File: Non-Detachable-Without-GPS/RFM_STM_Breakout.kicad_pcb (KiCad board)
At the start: 2 copper layers, 58 x 48.3 mm, 29 parts, among them J1 USB_B_Micro, J2 Conn_01x02_Male, J3 Conn_01x16_Male, J4 Conn_01x12_Male, J5 Conn_01x15_Male, J6 Conn_Coaxial, SW1 SW_Push, U1 RFM95W-868S2, U2 XC6206P332MR, U3 STM32L053R8Tx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

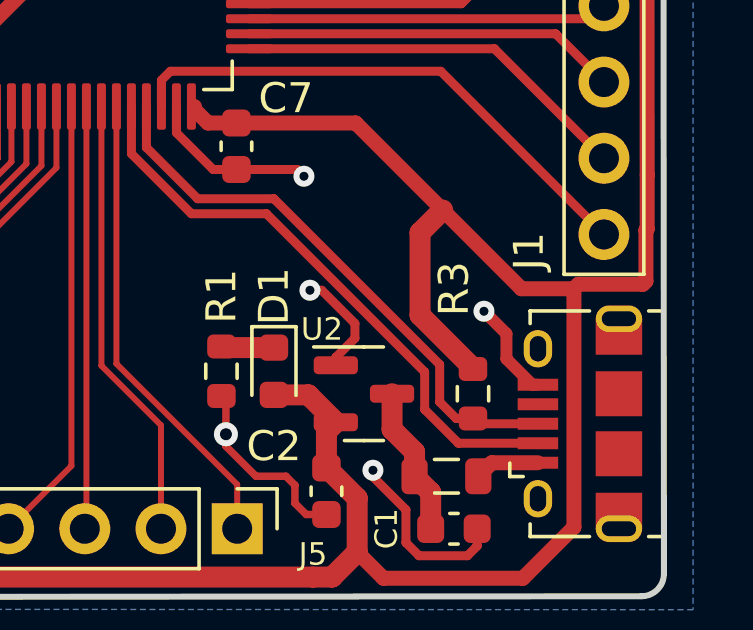
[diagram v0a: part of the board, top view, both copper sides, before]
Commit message: Update USB Pullup (R already internal in STM32L0 processors)
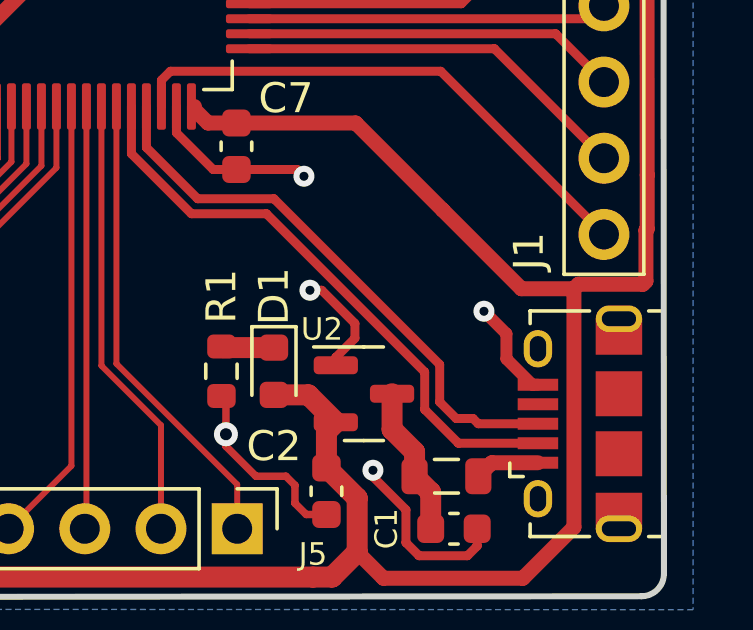
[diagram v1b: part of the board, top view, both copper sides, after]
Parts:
- removed R3: 1k5, Resistor_SMD:R_0603_1608Metric
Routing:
- net +3.3V: track 294.8 -> 288.5 mm
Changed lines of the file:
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@@
-    )
-  )
-  (footprint "Resistor_SMD:R_0603_1608Metric" (layer "F.Cu")
-    (at 131.635 105.25 -90)
-    (descr "Resistor SMD 0603 (1608 Metric), square (rectangular) end terminal, IPC_7351 nominal, (Body size source: IPC-SM-782 page 72, https://www.pcb-3d.com/wordpress/wp-content/uploads/ipc-sm-782a_amendment_1_and_2.pdf), generated with kicad-footprint-generator")
-    (tags "resistor")
-    (property "LCSC Part #" "C22842")
-    (property "Sheetfile" "RFM_STM_Breakout.kicad_sch")
-    (property "Sheetname" "")
-    (attr smd)
-    (fp_text reference "R3" (at -3.5 0.635 -90) (layer "F.SilkS")
-      (effects (font (size 1 1) (thickness 0.15)))
-    )
-    (fp_text value "1k5" (at 0 1.43 90) (layer "F.Fab") hide
-      (effects (font (size 1 1) (thickness 0.15)))
-    )
-    (fp_text user "${REFERENCE}" (at 0 0 90) (layer "F.Fab")
-      (effects (font (size 0.4 0.4) (thickness 0.06)))
-    )
-    (fp_line (start -0.237258 -0.5225) (end 0.237258 -0.5225) (layer "F.SilkS") (width 0.12))
-    (fp_line (start -0.237258 0.5225) (end 0.237258 0.5225) (layer "F.SilkS") (width 0.12))
-    (fp_line (start -1.48 -0.73) (end 1.48 -0.73) (layer "F.CrtYd") (width 0.05))
-    (fp_line (start -1.48 0.73) (end -1.48 -0.73) (layer "F.CrtYd") (width 0.05))
-    (fp_line (start 1.48 0.73) (end -1.48 0.73) (layer "F.CrtYd") (width 0.05))
-    (fp_line (start 1.48 -0.73) (end 1.48 0.73) (layer "F.CrtYd") (width 0.05))
-    (fp_line (start 0.8 -0.4125) (end 0.8 0.4125) (layer "F.Fab") (width 0.1))
-    (fp_line (start -0.8 -0.4125) (end 0.8 -0.4125) (layer "F.Fab") (width 0.1))
-    (fp_line (start 0.8 0.4125) (end -0.8 0.4125) (layer "F.Fab") (width 0.1))
-    (fp_line (start -0.8 0.4125) (end -0.8 -0.4125) (layer "F.Fab") (width 0.1))
-    (pad "1" smd roundrect (at -0.825 0 270) (size 0.8 0.95) (layers "F.Cu" "F.Paste" "F.Mask") (roundrect_rratio 0.25)
-      (net 1 "+3.3V") (pintype "passive"))
-    (pad "2" smd roundrect (at 0.825 0 270) (size 0.8 0.95) (layers "F.Cu" "F.Paste" "F.Mask") (roundrect_rratio 0.25)
-      (net 11 "USB_D+") (pintype "passive"))
-    (model "${KICAD6_3DMODEL_DIR}/Resistor_SMD.3dshapes/R_0603_1608Metric.wrl"
-      (offset (xyz 0 0 0))
-      (scale (xyz 1 1 1))
-      (rotate (xyz 0 0 0))
     )
   )
@@
   (segment (start 113.75 81.636396) (end 113.75 83.265) (width 0.3) (layer "F.Cu") (net 1))
   (segment (start 118.5 89.25) (end 118.5 89.2) (width 0.5) (layer "F.Cu") (net 1))
-  (segment (start 131.635 104.425) (end 131.635 104.39505) (width 0.7) (layer "F.Cu") (net 1))
   (segment (start 112.3 95) (end 113.5 95) (width 0.5) (layer "F.Cu") (net 1))
   (segment (start 129.75 64.5) (end 99.7 64.5) (width 0.3) (layer "F.Cu") (net 1))
@@
   (segment (start 129.6 66.9) (end 127 69.5) (width 0.7) (layer "F.Cu") (net 1))
   (segment (start 116.5 87.25) (end 118.5 89.25) (width 0.3) (layer "F.Cu") (net 1))
-  (segment (start 129.869975 99.880025) (end 130.625 99.125) (width 0.7) (layer "F.Cu") (net 1))
   (segment (start 126.299961 111.360841) (end 94.905841 111.360841) (width 0.7) (layer "F.Cu") (net 1))
-  (segment (start 131.635 104.39505) (end 129.869975 102.630025) (width 0.7) (layer "F.Cu") (net 1))
   (segment (start 137.4 101.5) (end 137.4 99.8) (width 0.5) (layer "F.Cu") (net 1))
   (segment (start 129.75 74.25) (end 133.5 70.5) (width 0.4) (layer "F.Cu") (net 1))
@@
   (segment (start 112.725 93.85) (end 112.825 93.85) (width 0.5) (layer "F.Cu") (net 1))
   (segment (start 137.433586 87.266414) (end 137.433586 85.966603) (width 0.5) (layer "F.Cu") (net 1))
-  (segment (start 129.869975 102.630025) (end 129.869975 99.880025) (width 0.7) (layer "F.Cu") (net 1))
   (segment (start 127.725 96.225) (end 130.625 99.125) (width 0.5) (layer "F.Cu") (net 1))
   (segment (start 95.835 107.135) (end 95.835 109.75) (width 0.7) (layer "F.Cu") (net 1))
